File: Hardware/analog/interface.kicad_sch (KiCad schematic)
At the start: 24 parts

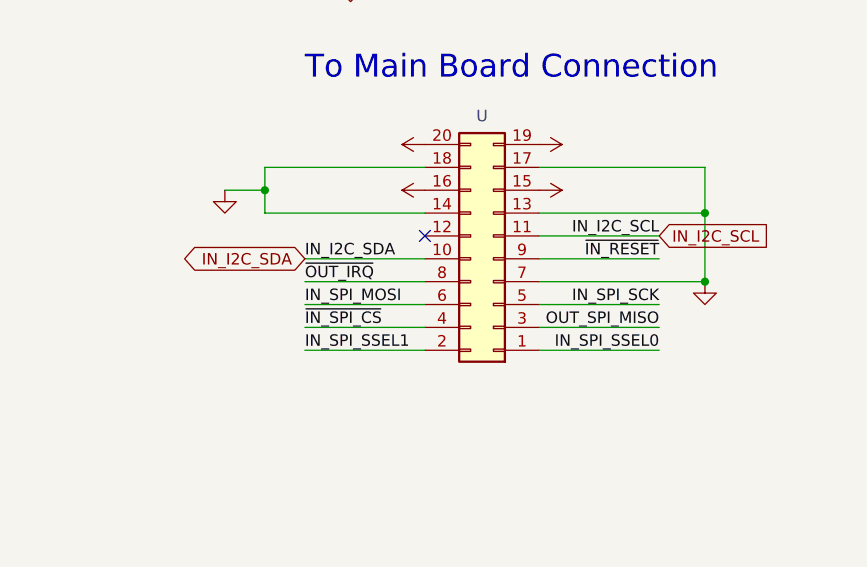
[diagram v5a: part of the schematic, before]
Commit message: More reworking of the controller and friends
- Add more rear IO to the controller, in this case finishing positioning
  of the Ethernet jack, and adding a suitable right angle USB B jack
  (USB C is preferrable but there's basically no jacks that are
  sufficiently long)

- Mostly finish power section on controller (save for the enable input
  for our +3V3 rail; it'll be slaved off the SoM +3V3 rail)

- Minor tweaks to pinout of FFC connector on front panel

- Update cutout shape of analog board

- Fixed a few footprints metadata

- Add footprints for further rear panel IO
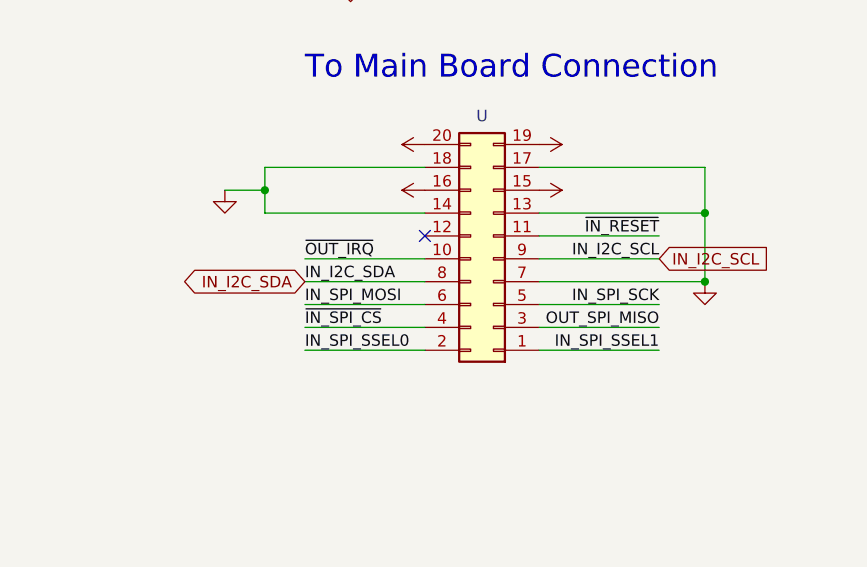
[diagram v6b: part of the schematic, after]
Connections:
- net IN_I2C_SCL: now also U.9 (Pin_9); no longer U.11 (Pin_11)
- net IN_I2C_SDA: now also U.8 (Pin_8); no longer U.10 (Pin_10)
- net IN_SPI_SSEL0: now also U.2 (Pin_2); no longer U.1 (Pin_1)
- net IN_SPI_SSEL1: now also U.1 (Pin_1); no longer U.2 (Pin_2)
- net ~{IN_RESET}: now also U.11 (Pin_11); no longer U.9 (Pin_9)
- net ~{OUT_IRQ}: now also U.10 (Pin_10); no longer U.8 (Pin_8)

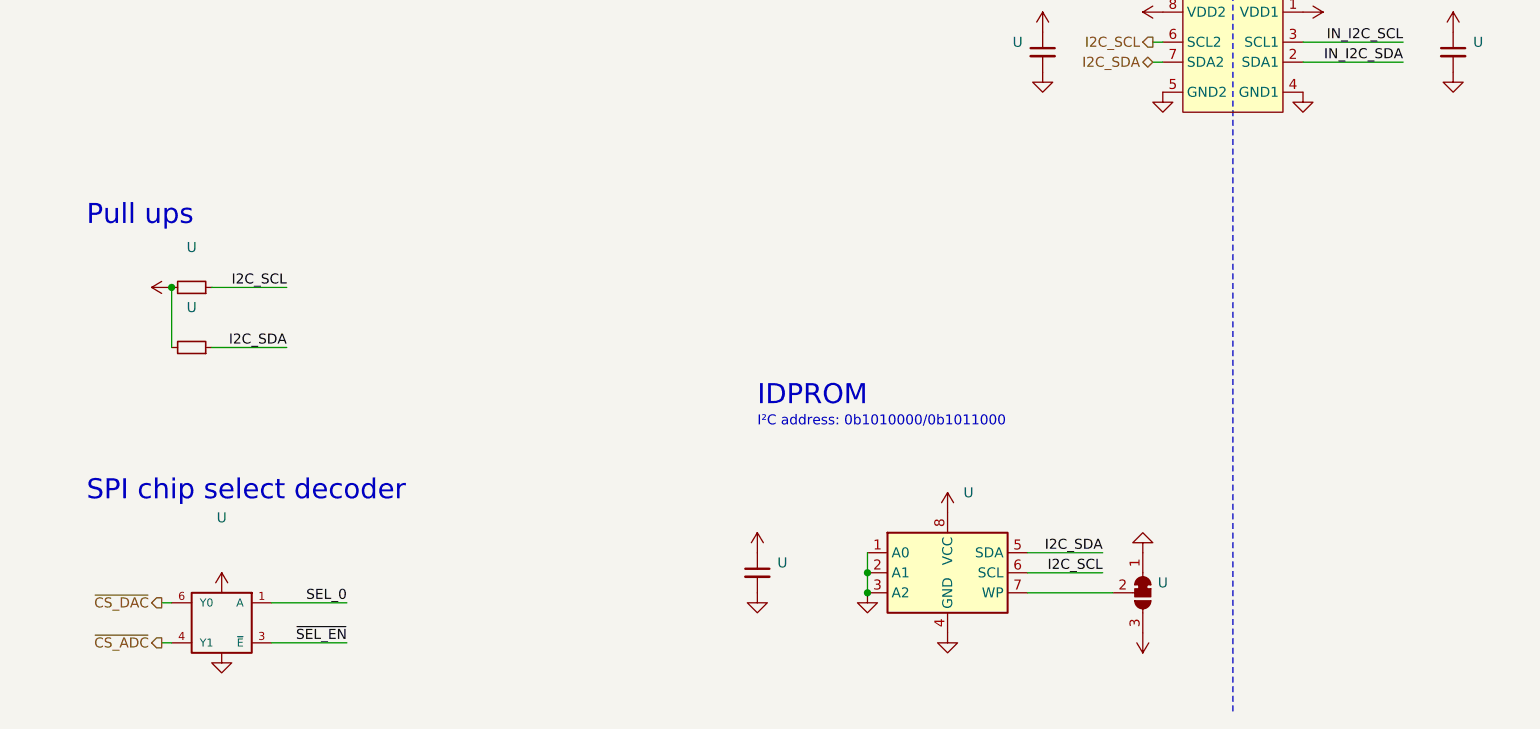
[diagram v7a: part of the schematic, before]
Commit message: Analog board layout
- Started work on adding the voltage sense circuitry, including the
  selector relay, IO expander to drive the relay, and the second ADC to
  convert the voltage values

- Changed the layout of analog board to better take advantage of
  available space

- Minor changes to front panel layout for aesthetics
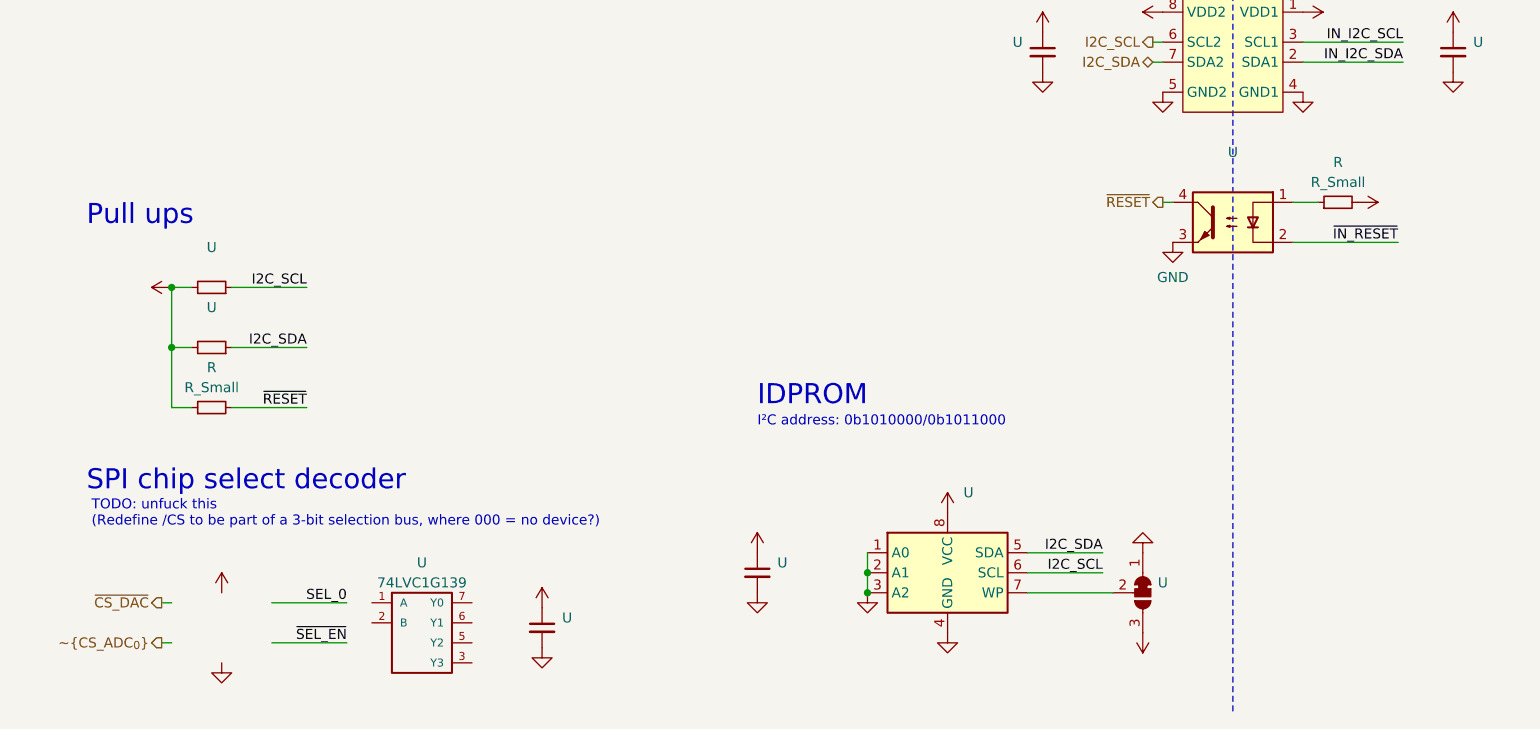
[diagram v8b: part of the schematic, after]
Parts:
- removed U: (no value), symbol 74xGxx:74LVC1G19
- added R (x2): R_Small, symbol Device:R_Small
- added U: (no value), symbol Device:C_Small
- added U: 74LVC1G139, symbol 74xGxx:74LVC1G139
- added U: (no value), symbol Isolator:FODM217B
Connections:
- net +3.3VP: now also R.2
- net +3V3: now also R.1, U.1
- net GND: now also U.2, U.3, U.4 (GND)
- net ~{IN_RESET}: now also U.2
- new net: R.1, U.1
- new net VCC: U.8 (VCC)
- new net ~{RESET}: R.2, U.4
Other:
- note added: "TODO: unfuck this (Redefine /CS to be part of a 3-bit selection bus, where 000 = no device?)"
- moved on the sheet: U
